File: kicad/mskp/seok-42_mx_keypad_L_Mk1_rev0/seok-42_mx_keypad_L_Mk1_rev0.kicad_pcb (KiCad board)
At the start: 2 copper layers, 43 parts, among them J1 Conn_01x12_Socket, SW1 Switch, SW10 Switch, SW11 Switch, SW12 Switch, SW13 Switch, SW14 Switch, SW15 Switch, SW16 Switch, SW17 Switch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

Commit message: Minor keypad design update ideas
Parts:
- moved J1 15.4 mm to (191.3, 96.8)
- moved D11 13.6 mm to (216.5, 73.0)
- moved D18 13.6 mm to (227.2, 73.0)
- moved D10 13.6 mm to (216.5, 69.4)
- moved D12 13.6 mm to (216.5, 76.5)
- moved D13 13.6 mm to (216.5, 80.1)
- moved D14 13.6 mm to (216.5, 83.6)
- moved D15 13.6 mm to (227.2, 62.3)
- moved D16 13.6 mm to (227.2, 65.9)
- moved D17 13.6 mm to (227.2, 69.4)
- moved D19 13.6 mm to (227.2, 76.5)
- moved D20 13.6 mm to (227.2, 80.1)
- moved D21 13.6 mm to (227.2, 83.6)
- moved D8 13.6 mm to (216.5, 62.3)
- moved D9 13.6 mm to (216.5, 65.9)
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
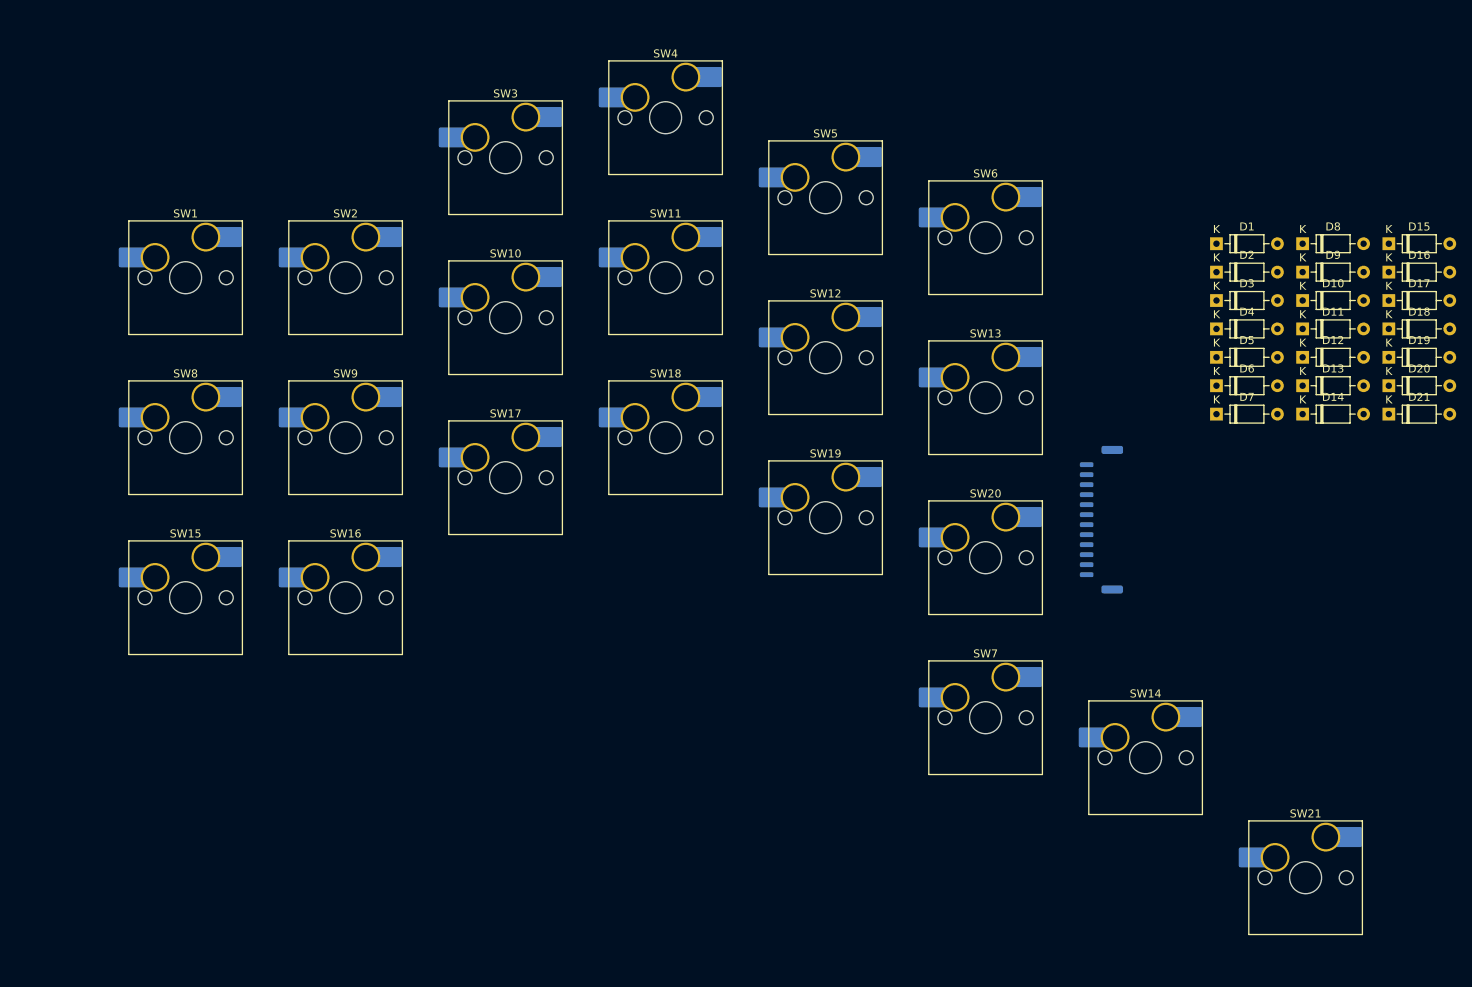
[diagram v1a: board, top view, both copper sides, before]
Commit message: Add diodes positions to seok-42_mx_keypad_L_Mk1_rev0
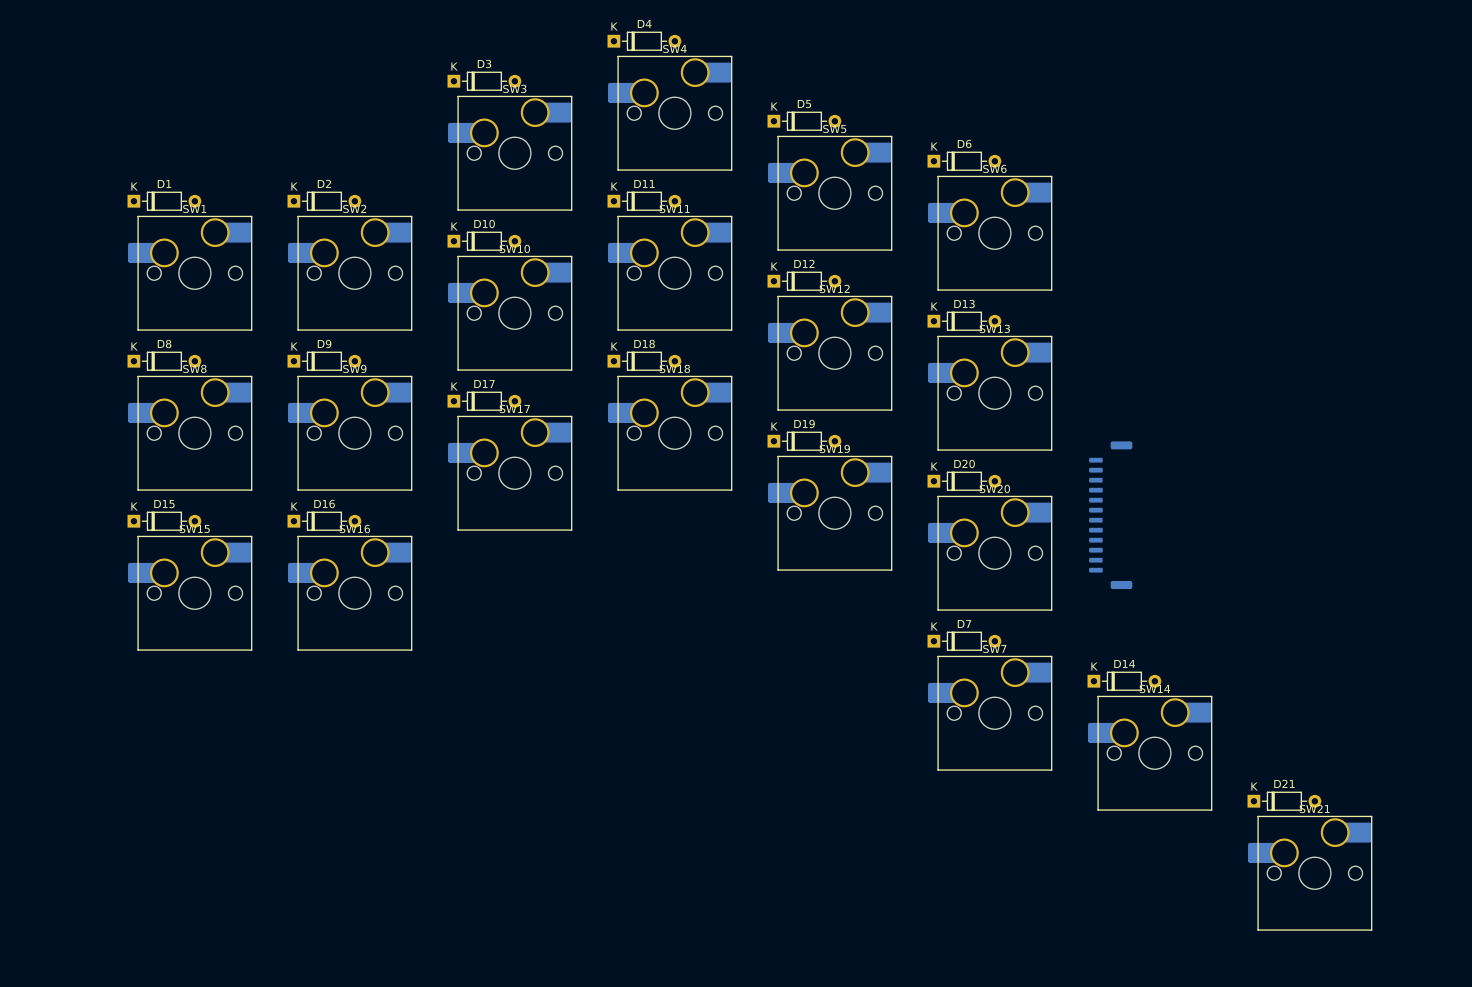
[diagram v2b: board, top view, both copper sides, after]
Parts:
- moved D15 160.7 mm to (70.4, 97.0)
- moved D8 146.8 mm to (70.4, 77.0)
- moved D16 140.4 mm to (90.4, 97.0)
- moved D1 135.4 mm to (70.4, 57.0)
- moved D9 126.6 mm to (90.4, 77.0)
- moved D17 117.5 mm to (110.4, 82.0)
- moved D2 115.7 mm to (90.4, 57.0)
- moved D10 106.3 mm to (110.4, 62.0)
- moved D3 99.2 mm to (110.4, 42.0)
- moved D18 96.9 mm to (130.4, 77.0)
- moved D11 87.6 mm to (130.4, 57.0)
- moved D4 83.5 mm to (130.4, 37.0)
- moved D19 77.6 mm to (150.4, 87.0)
- moved D12 66.8 mm to (150.4, 67.0)
- moved D5 62.7 mm to (150.4, 47.0)
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
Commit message: Add initial board outline for seok-42_mx_keypad_L_Mk1_rev0
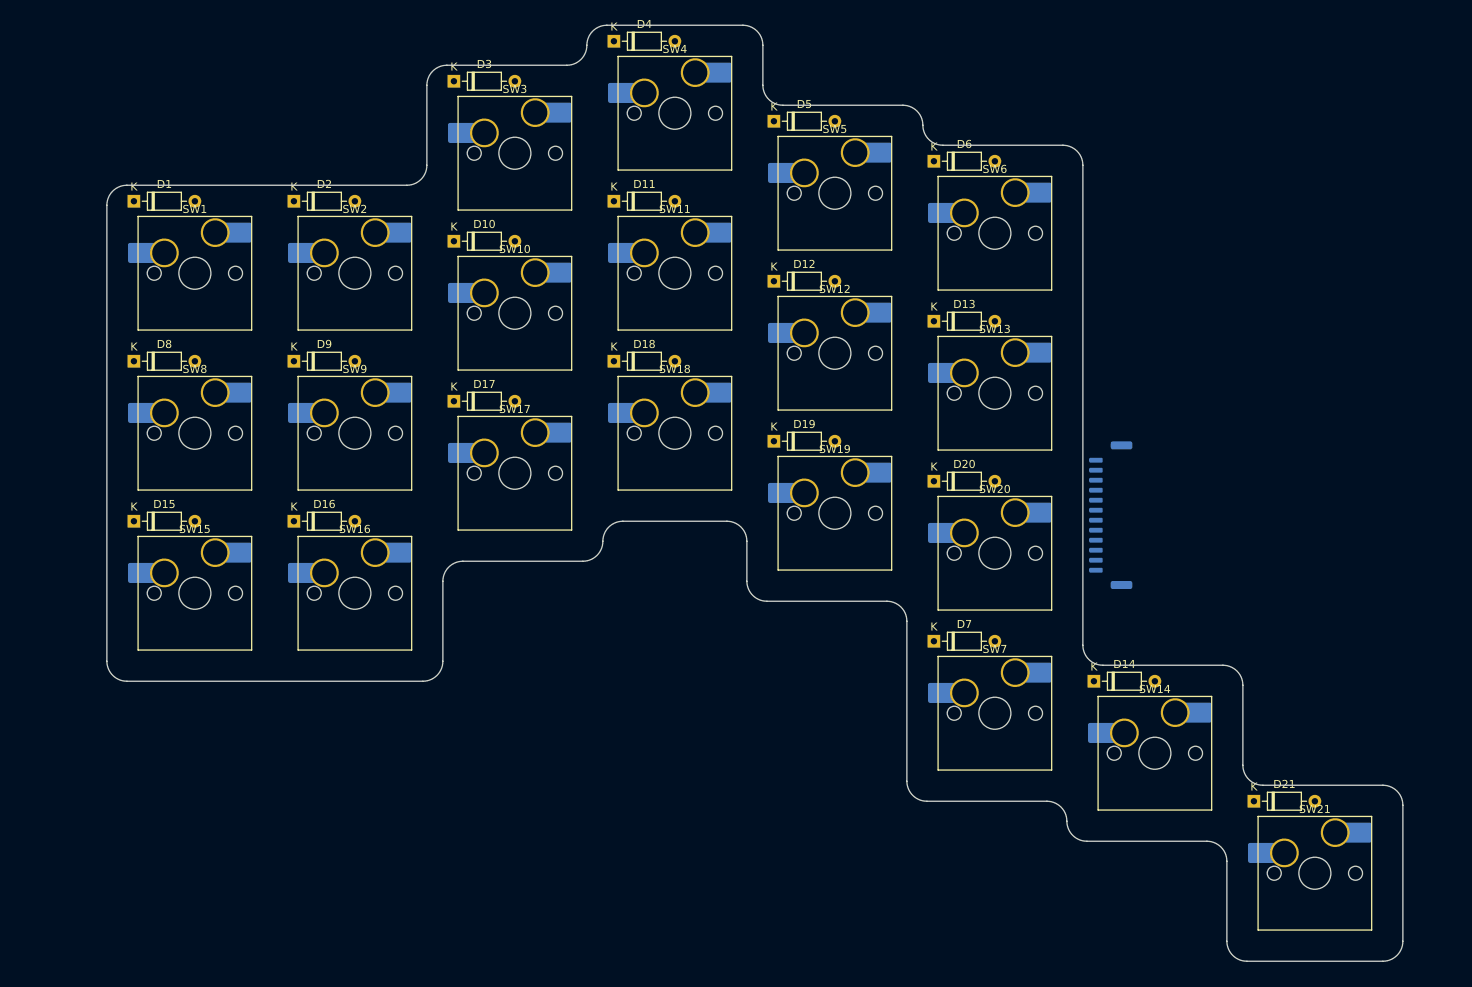
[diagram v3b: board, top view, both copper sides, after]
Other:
- board outline added: 162 x 117 mm
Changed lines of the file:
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@@
     )
   )
+  (gr_arc (start 226.5 130) (mid 228.267767 130.732233) (end 229 132.5)
+    (stroke (width 0.1) (type default)) (layer "Edge.Cuts"))
+  (gr_line (start 151.5 45) (end 166.5 45)
+    (stroke (width 0.1) (type default)) (layer "Edge.Cuts"))
+  (gr_arc (start 107 42.5) (mid 107.732233 40.732233) (end 109.5 40)
+    (stroke (width 0.1) (type default)) (layer "Edge.Cuts"))
+  (gr_arc (start 164.5 107) (mid 166.267767 107.732233) (end 167 109.5)
+    (stroke (width 0.1) (type default)) (layer "Edge.Cuts"))
+  (gr_arc (start 204.5 137) (mid 206.267767 137.732233) (end 207 139.5)
+    (stroke (width 0.1) (type default)) (layer "Edge.Cuts"))
+  (gr_arc (start 127 37.5) (mid 126.267767 39.267767) (end 124.5 40)
+    (stroke (width 0.1) (type default)) (layer "Edge.Cuts"))
+  (gr_line (start 127 37.5) (end 127 37.5)
+    (stroke (width 0.1) (type default)) (layer "Edge.Cuts"))
+  (gr_arc (start 129 99.5) (mid 129.732233 97.732233) (end 131.5 97)
+    (stroke (width 0.1) (type default)) (layer "Edge.Cuts"))
+  (gr_arc (start 69.5 117) (mid 67.732233 116.267767) (end 67 114.5)
+    (stroke (width 0.1) (type default)) (layer "Edge.Cuts"))
+  (gr_line (start 69.5 55) (end 104.5 55)
+    (stroke (width 0.1) (type default)) (layer "Edge.Cuts"))
+  (gr_line (start 171.5 50) (end 186.5 50)
+    (stroke (width 0.1) (type default)) (layer "Edge.Cuts"))
+  (gr_line (start 144.5 97) (end 131.5 97)
+    (stroke (width 0.1) (type default)) (layer "Edge.Cuts"))
+  (gr_arc (start 169.5 132) (mid 167.732233 131.267767) (end 167 129.5)
+    (stroke (width 0.1) (type default)) (layer "Edge.Cuts"))
+  (gr_line (start 126.5 102) (end 111.5 102)
+    (stroke (width 0.1) (type default)) (layer "Edge.Cuts"))
+  (gr_line (start 149 37.5) (end 149 42.5)
+    (stroke (width 0.1) (type default)) (layer "Edge.Cuts"))
+  (gr_line (start 129.5 35) (end 146.5 35)
+    (stroke (width 0.1) (type default)) (layer "Edge.Cuts"))
+  (gr_line (start 109.5 40) (end 124.5 40)
+    (stroke (width 0.1) (type default)) (layer "Edge.Cuts"))
+  (gr_line (start 109 104.5) (end 109 114.5)
+    (stroke (width 0.1) (type default)) (layer "Edge.Cuts"))
+  (gr_line (start 187 134.5) (end 187 134.5)
+    (stroke (width 0.1) (type default)) (layer "Edge.Cuts"))
+  (gr_arc (start 107 52.5) (mid 106.267767 54.267767) (end 104.5 55)
+    (stroke (width 0.1) (type default)) (layer "Edge.Cuts"))
+  (gr_arc (start 144.5 97) (mid 146.267767 97.732233) (end 147 99.5)
+    (stroke (width 0.1) (type default)) (layer "Edge.Cuts"))
+  (gr_line (start 147 104.5) (end 147 99.5)
+    (stroke (width 0.1) (type default)) (layer "Edge.Cuts"))
+  (gr_line (start 189 52.5) (end 189 112.5)
+    (stroke (width 0.1) (type default)) (layer "Edge.Cuts"))
+  (gr_line (start 164.5 107) (end 149.5 107)
+    (stroke (width 0.1) (type default)) (layer "Edge.Cuts"))
+  (gr_arc (start 146.5 35) (mid 148.267767 35.732233) (end 149 37.5)
+    (stroke (width 0.1) (type default)) (layer "Edge.Cuts"))
+  (gr_line (start 204.5 137) (end 189.5 137)
+    (stroke (width 0.1) (type default)) (layer "Edge.Cuts"))
+  (gr_arc (start 171.5 50) (mid 169.732233 49.267767) (end 169 47.5)
+    (stroke (width 0.1) (type default)) (layer "Edge.Cuts"))
+  (gr_line (start 207 149.5) (end 207 139.5)
+    (stroke (width 0.1) (type default)) (layer "Edge.Cuts"))
+  (gr_arc (start 189.5 137) (mid 187.732233 136.267767) (end 187 134.5)
+    (stroke (width 0.1) (type default)) (layer "Edge.Cuts"))
+  (gr_line (start 211.5 130) (end 226.5 130)
+    (stroke (width 0.1) (type default)) (layer "Edge.Cuts"))
+  (gr_arc (start 186.5 50) (mid 188.267767 50.732233) (end 189 52.5)
+    (stroke (width 0.1) (type default)) (layer "Edge.Cuts"))
+  (gr_arc (start 149.5 107) (mid 147.732233 106.267767) (end 147 104.5)
+    (stroke (width 0.1) (type default)) (layer "Edge.Cuts"))
+  (gr_arc (start 206.5 115) (mid 208.267767 115.732233) (end 209 117.5)
+    (stroke (width 0.1) (type default)) (layer "Edge.Cuts"))
+  (gr_line (start 107 52.5) (end 107 42.5)
+    (stroke (width 0.1) (type default)) (layer "Edge.Cuts"))
+  (gr_arc (start 209.5 152) (mid 207.732233 151.267767) (end 207 149.5)
+    (stroke (width 0.1) (type default)) (layer "Edge.Cuts"))
+  (gr_line (start 191.5 115) (end 206.5 115)
+    (stroke (width 0.1) (type default)) (layer "Edge.Cuts"))
+  (gr_arc (start 109 104.5) (mid 109.732233 102.732233) (end 111.5 102)
+    (stroke (width 0.1) (type default)) (layer "Edge.Cuts"))
+  (gr_line (start 129 99.5) (end 129 99.5)
+    (stroke (width 0.1) (type default)) (layer "Edge.Cuts"))
+  (gr_arc (start 184.5 132) (mid 186.267767 132.732233) (end 187 134.5)
+    (stroke (width 0.1) (type default)) (layer "Edge.Cuts"))
+  (gr_line (start 67 114.5) (end 67 57.5)
+    (stroke (width 0.1) (type default)) (layer "Edge.Cuts"))
+  (gr_line (start 229 132.5) (end 229 149.5)
+    (stroke (width 0.1) (type default)) (layer "Edge.Cuts"))
+  (gr_line (start 169 47.5) (end 169 47.5)
+    (stroke (width 0.1) (type default)) (layer "Edge.Cuts"))
+  (gr_line (start 167 129.5) (end 167 109.5)
+    (stroke (width 0.1) (type default)) (layer "Edge.Cuts"))
+  (gr_arc (start 109 114.5) (mid 108.267767 116.267767) (end 106.5 117)
+    (stroke (width 0.1) (type default)) (layer "Edge.Cuts"))
+  (gr_arc (start 67 57.5) (mid 67.732233 55.732233) (end 69.5 55)
+    (stroke (width 0.1) (type default)) (layer "Edge.Cuts"))
+  (gr_line (start 226.5 152) (end 209.5 152)
+    (stroke (width 0.1) (type default)) (layer "Edge.Cuts"))
+  (gr_line (start 209 117.5) (end 209 127.5)
+    (stroke (width 0.1) (type default)) (layer "Edge.Cuts"))
+  (gr_arc (start 229 149.5) (mid 228.267767 151.267767) (end 226.5 152)
+    (stroke (width 0.1) (type default)) (layer "Edge.Cuts"))
+  (gr_arc (start 127 37.5) (mid 127.732233 35.732233) (end 129.5 35)
+    (stroke (width 0.1) (type default)) (layer "Edge.Cuts"))
+  (gr_arc (start 211.5 130) (mid 209.732233 129.267767) (end 209 127.5)
+    (stroke (width 0.1) (type default)) (layer "Edge.Cuts"))
+  (gr_arc (start 151.5 45) (mid 149.732233 44.267767) (end 149 42.5)
+    (stroke (width 0.1) (type default)) (layer "Edge.Cuts"))
+  (gr_arc (start 166.5 45) (mid 168.267767 45.732233) (end 169 47.5)
+    (stroke (width 0.1) (type default)) (layer "Edge.Cuts"))
+  (gr_arc (start 129 99.5) (mid 128.267767 101.267767) (end 126.5 102)
+    (stroke (width 0.1) (type default)) (layer "Edge.Cuts"))
+  (gr_line (start 184.5 132) (end 169.5 132)
+    (stroke (width 0.1) (type default)) (layer "Edge.Cuts"))
+  (gr_arc (start 191.5 115) (mid 189.732233 114.267767) (end 189 112.5)
+    (stroke (width 0.1) (type default)) (layer "Edge.Cuts"))
+  (gr_line (start 106.5 117) (end 69.5 117)
+    (stroke (width 0.1) (type default)) (layer "Edge.Cuts"))
   (dimension (type aligned) (layer "F.Cu")
     (pts (xy 98 66) (xy 98 55))

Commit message: Minor pcb updates for qlp and seok keypads
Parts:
- added REF**: MountingHole_2.2mm_M2_ISO14580, MountingHole:MountingHole_2.2mm_M2_ISO14580, F.Cu at (207.0, 71.0)
